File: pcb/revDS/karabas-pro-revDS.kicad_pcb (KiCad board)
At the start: 2 copper layers, 101.6 x 147.3 mm, 212 parts, among them CON1 CF-CARD, CON2 SD, CON3 VGA, CON4 Joystick, CON5 Keyboard, CON6 Mouse, CON7 Audio, CON8 12V, CON9 MicroSD', J1 Floppy, J10 Ext Joystick, J2 FPGA JTAG, J3 Floppy, J4 uBus, J5 AVR JTAG, J6 AVR UART, J7 ESP-BUS, J8 Tape In, J9 Tape Out, Q1 BC856, SW1 SW_Push, SW2 SW_Push, SW4 SW_SPST, U1 EP4CE6E22C8N, U10 ESP-12E, U11 TDA1543, U12 AMS1117-3.3, U13 AMS1117-2.5, U14 AMS1117-1.2, U15 LM2596S-5, U16 LM311, U17 74LS06, U18 74LS38, U2 CY62167EV30, U3 W25Q16, U3''1 W25Q16, U4 EPM3128ATC100-5, U5 ATMEGA328-AU, U6 MB8877A, U7 TXB0104PW, U8 TXB0104PW, U9 DS1307Z+, X1 SG-7050CAN, Y1 32768Hz, Y2 16MHz

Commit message: Updated pcb rev.DS
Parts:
- added G***: LOGO, footprints:karabas_pro_logo2-coppermask, F.Cu at (133.2, 163.9)
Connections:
- net Net-(D1-Pad2) renamed /L1
- net Net-(D2-Pad2) renamed /L2
- net Net-(D4-Pad1) renamed /L4
- net Net-(D6-Pad1) renamed /L5
- net Net-(D7-Pad2) renamed /L3
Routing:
- net VCC1_2: track 132.3 -> 132.9 mm
- net /PIN_25: track 31.7 -> 32.3 mm

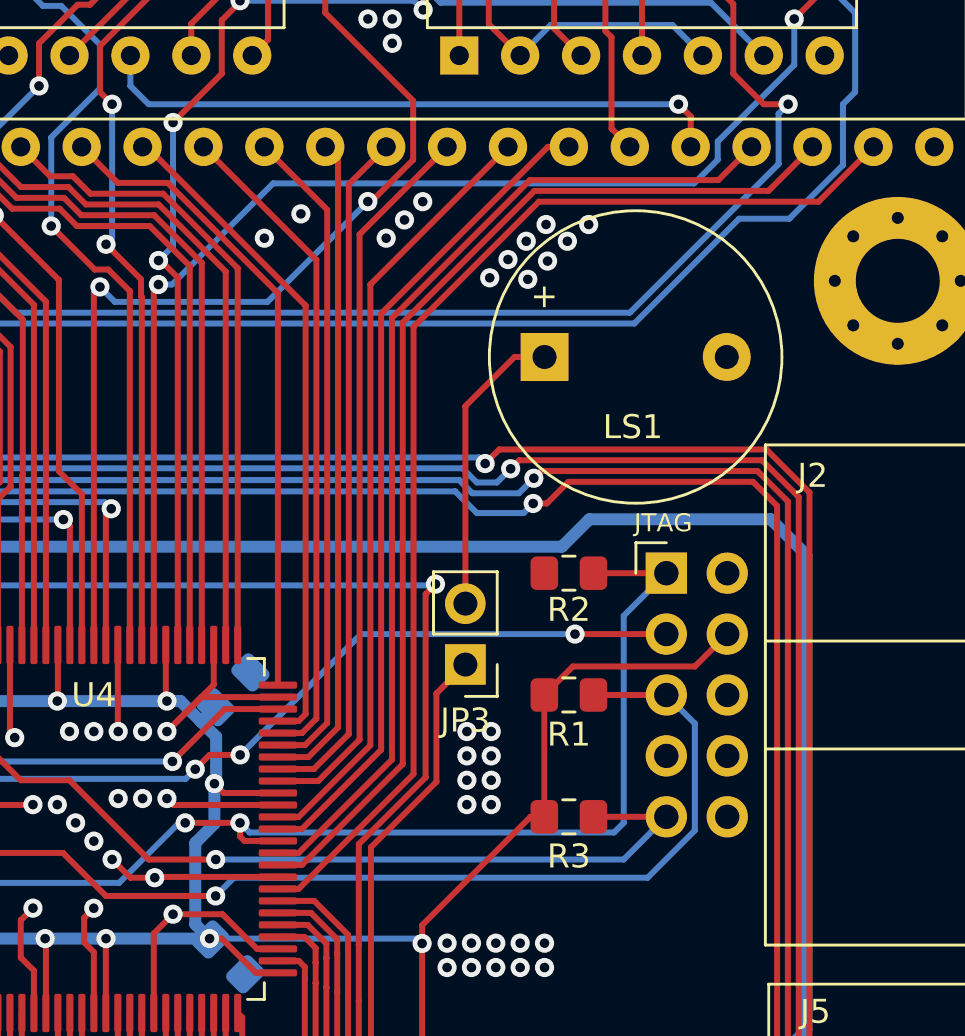
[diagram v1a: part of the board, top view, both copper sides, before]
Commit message: updated revDS: added diode and transistor before buzzer
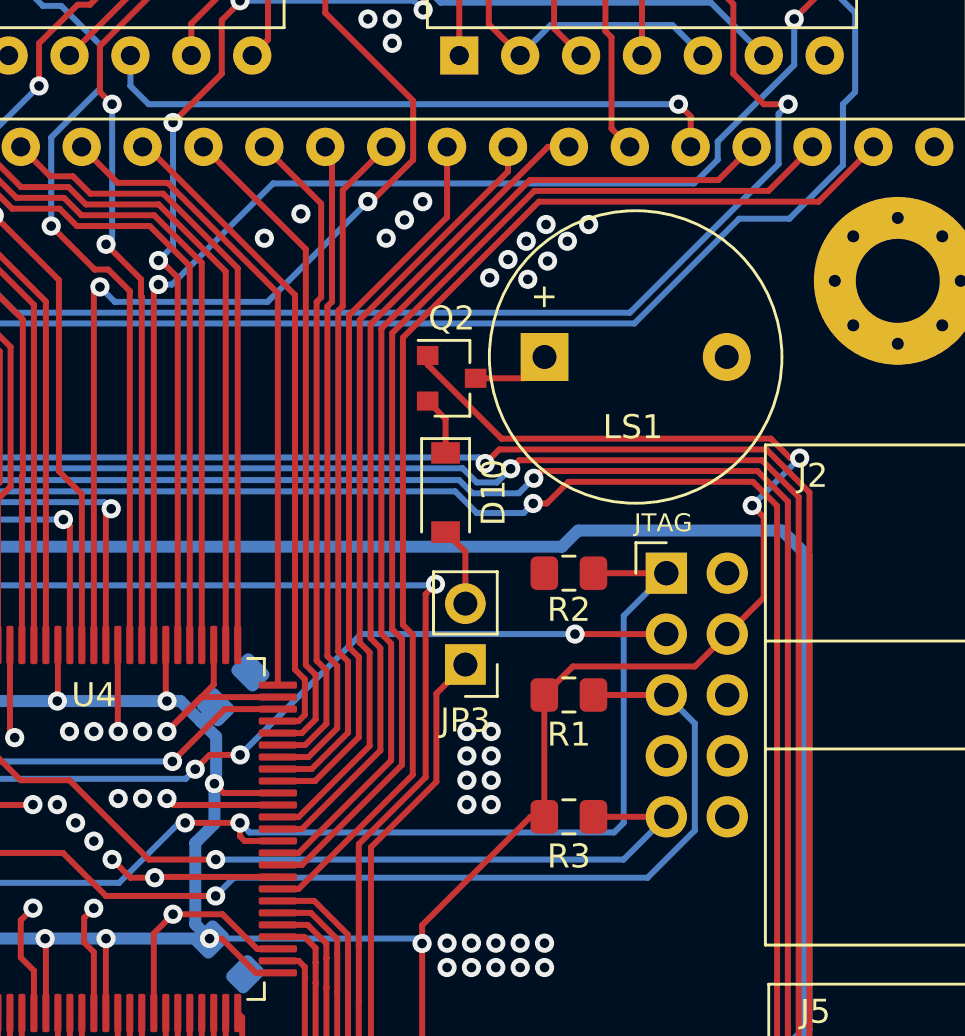
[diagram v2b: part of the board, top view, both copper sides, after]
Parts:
- removed the G*** at (133.2, 163.9)
- added D10: 1N4148W, Diode_SMD:D_SOD-123, F.Cu at (177.7, 79.4)
- added Q2: BC548, Package_TO_SOT_SMD:SOT-23, F.Cu at (178.0, 74.7)
- U1: value EP4CE6E22C8N -> EP4CE10E22C8N
- U2: value CY62167EV30 -> CY62167EV30LL
- U4: value EPM3128ATC100-5 -> EPM3128ATC100-10N
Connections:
- JP3 pad 2: Net-(JP3-Pad2) -> Net-(D10-Pad2)
- LS1 pad 1: Net-(JP3-Pad2) -> Net-(LS1-Pad1)
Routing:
- net VCC3_3: track 616.0 -> 642.5 mm, vias 39 -> 41
- net Net-(JP3-Pad2): track 13.1 -> 0.00 mm
- net Net-(LS1-Pad1): track 0.00 -> 3.75 mm
- net Net-(D10-Pad2): track 0.00 -> 3.33 mm
- net Net-(D10-Pad1): track 0.00 -> 2.47 mm

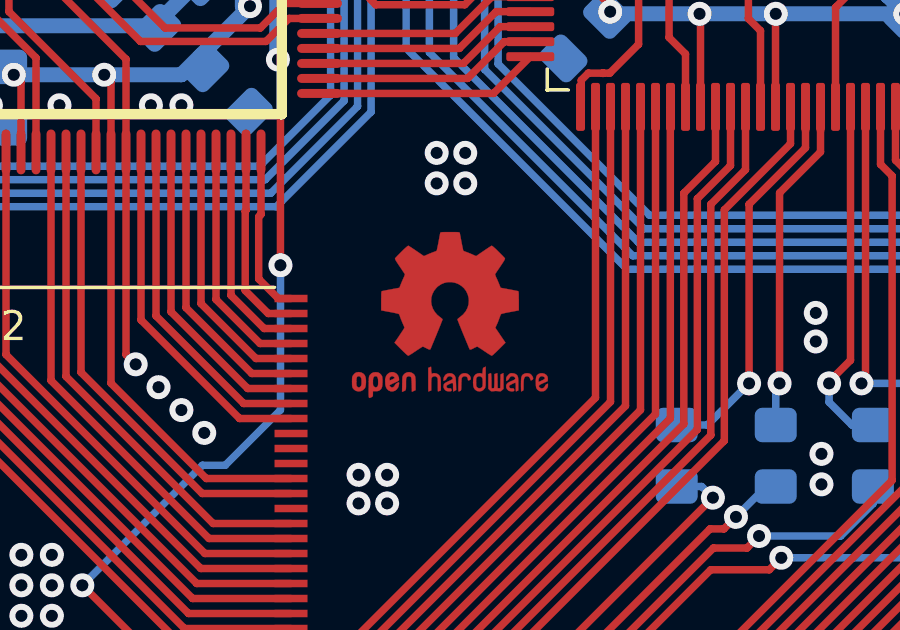
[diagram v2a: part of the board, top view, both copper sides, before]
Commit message: OSH logo - mask
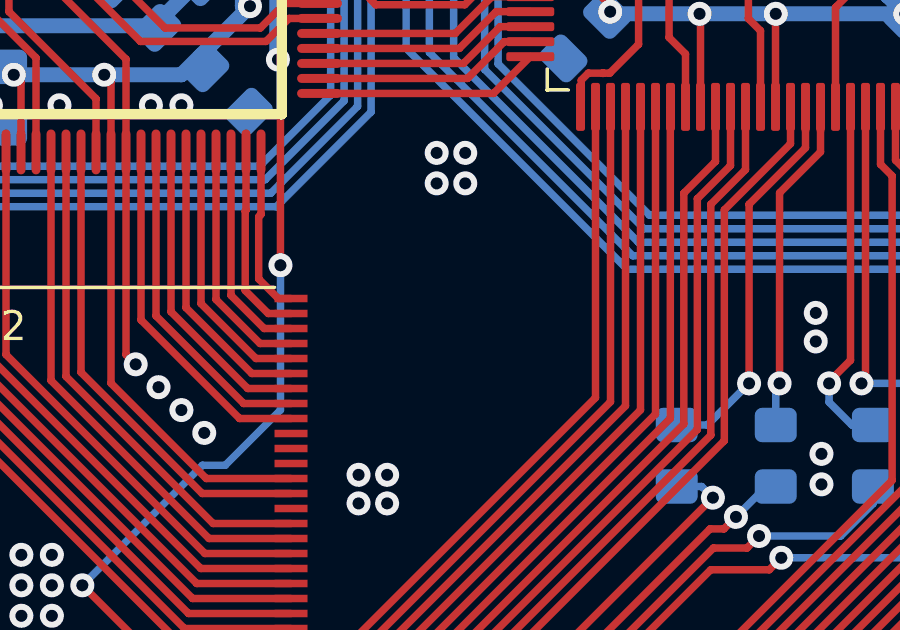
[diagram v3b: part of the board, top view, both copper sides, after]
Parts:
- REF**: value OSHW-Logo2_7.3x6mm_Copper -> OSHW-Logo2_7.3x6mm_Mask; footprint Symbol:OSHW-Logo2_7.3x6mm_Copper -> footprints:OSHW-Logo2_7.3x6mm_Mask

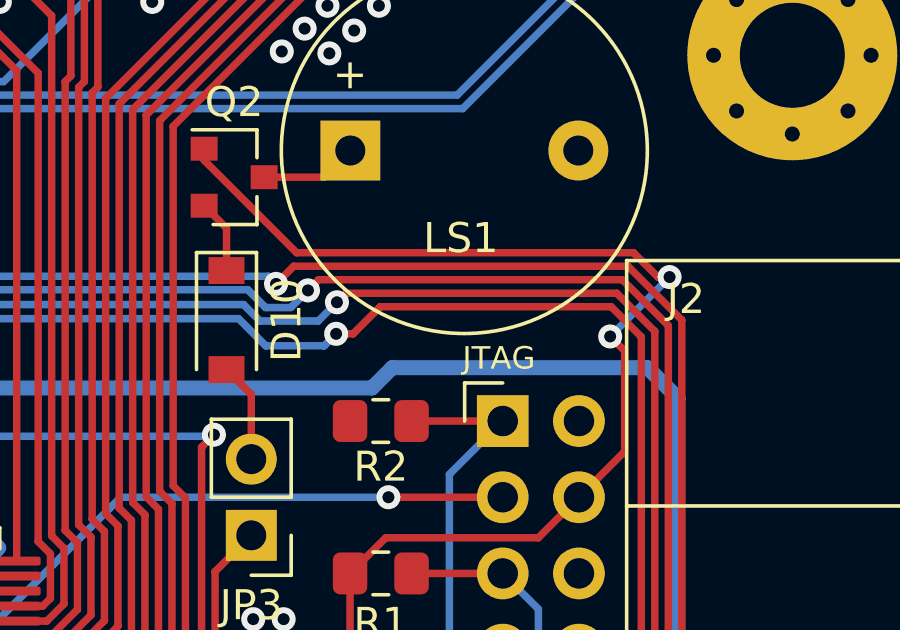
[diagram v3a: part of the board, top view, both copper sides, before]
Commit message: Added missing R for buzzer
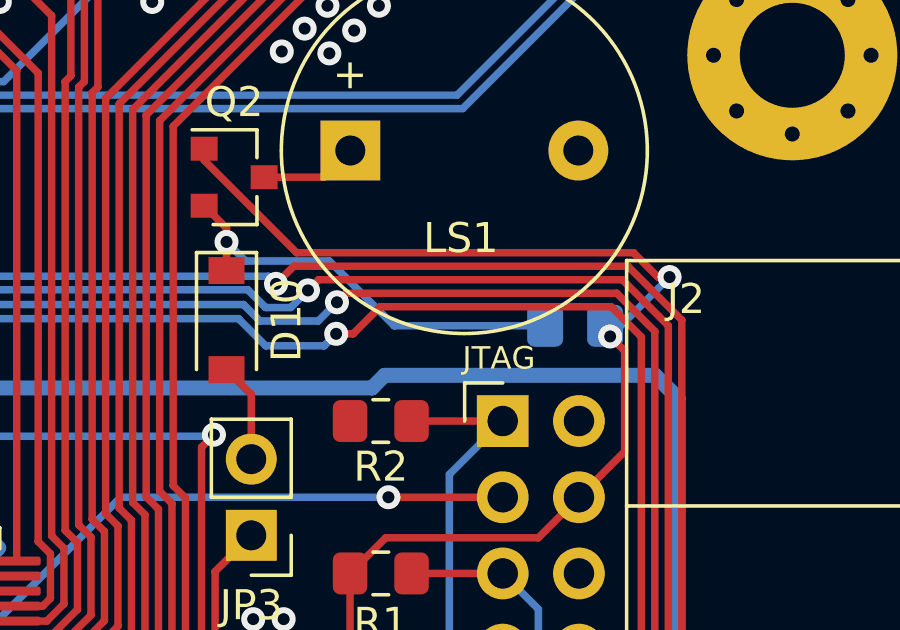
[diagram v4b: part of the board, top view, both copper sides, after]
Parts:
- added R48: 1k, Resistor_SMD:R_0805_2012Metric_Pad1.20x1.40mm_HandSolder, B.Cu at (189.4, 79.6)
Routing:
- net Net-(D10-Pad1): track 2.47 -> 14.2 mm, vias 0 -> 1

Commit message: latest version
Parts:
- added C59: 1uF, Capacitor_SMD:C_0805_2012Metric_Pad1.18x1.45mm_HandSolder, F.Cu at (216.3, 124.6)
- added C60: 1uF, Capacitor_SMD:C_0805_2012Metric_Pad1.18x1.45mm_HandSolder, F.Cu at (221.2, 124.6)
- added C61: 1uF, Capacitor_SMD:C_0805_2012Metric_Pad1.18x1.45mm_HandSolder, F.Cu at (216.3, 127.6)
- added C62: 1uF, Capacitor_SMD:C_0805_2012Metric_Pad1.18x1.45mm_HandSolder, F.Cu at (221.2, 127.6)
- added U19: AMS1117-3.3, Package_TO_SOT_SMD:TO-252-2, F.Cu at (220.0, 119.1)
- added U20: AMS1117-3.3, Package_TO_SOT_SMD:TO-252-2, F.Cu at (232.2, 119.1)
- C27: moved to F.Cu
- moved C27 11.3 mm to (124.7, 113.0), turned to 225 degrees
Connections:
- C13 pad 1: VCC3_3 -> /+3.3ESP
- C18 pad 1: VCC3_3 -> /+3.3ESP
- C54 pad 1: VCC3_3 -> /+3.3ESP
- CON1 pad 13: VCC3_3 -> +3.3VP
- CON1 pad 38: VCC3_3 -> +3.3VP
- CON2 pad 4: VCC3_3 -> +3.3VP
- CON9 pad 4: VCC3_3 -> +3.3VP
- D4 pad 2: VCC3_3 -> +3.3VP
- D6 pad 2: VCC3_3 -> +3.3VP
- J7 pad 10: VCC3_3 -> /+3.3ESP
- R30 pad 2: VCC3_3 -> /+3.3ESP
- R31 pad 2: VCC3_3 -> /+3.3ESP
- R36 pad 2: VCC3_3 -> +3.3VP
- R37 pad 1: VCC3_3 -> +3.3VP
- R52 pad 2: VCC3_3 -> +3.3VP
- R74 pad 1: VCC3_3 -> +3.3VP
- R75 pad 1: VCC3_3 -> +3.3VP
- U10 pad 8: VCC3_3 -> /+3.3ESP
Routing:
- net VCC3_3: track 642.5 -> 405.1 mm, vias 41 -> 29
- net +3.3VP: track 0.00 -> 84.5 mm, vias 0 -> 3
- net /+3.3ESP: track 0.00 -> 45.1 mm
- net VCC: track 650.9 -> 651.4 mm

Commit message: Revert "latest version"
This reverts commit fe14166d25968ab133076a7a9191b22261ce910e.
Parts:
- removed C59, C60, C61, C62: 1uF, Capacitor_SMD:C_0805_2012Metric_Pad1.18x1.45mm_HandSolder
- removed U19, U20: AMS1117-3.3, Package_TO_SOT_SMD:TO-252-2
- C27: moved to B.Cu
- moved C27 11.3 mm to (135.3, 117.0), turned to 90 degrees
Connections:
- C13 pad 1: /+3.3ESP -> VCC3_3
- C18 pad 1: /+3.3ESP -> VCC3_3
- C54 pad 1: /+3.3ESP -> VCC3_3
- CON1 pad 13: +3.3VP -> VCC3_3
- CON1 pad 38: +3.3VP -> VCC3_3
- CON2 pad 4: +3.3VP -> VCC3_3
- CON9 pad 4: +3.3VP -> VCC3_3
- D4 pad 2: +3.3VP -> VCC3_3
- D6 pad 2: +3.3VP -> VCC3_3
- J7 pad 10: /+3.3ESP -> VCC3_3
- R30 pad 2: /+3.3ESP -> VCC3_3
- R31 pad 2: /+3.3ESP -> VCC3_3
- R36 pad 2: +3.3VP -> VCC3_3
- R37 pad 1: +3.3VP -> VCC3_3
- R52 pad 2: +3.3VP -> VCC3_3
- R74 pad 1: +3.3VP -> VCC3_3
- R75 pad 1: +3.3VP -> VCC3_3
- U10 pad 8: /+3.3ESP -> VCC3_3
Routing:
- net VCC3_3: track 405.1 -> 642.5 mm, vias 29 -> 41
- net +3.3VP: track 84.5 -> 0.00 mm, vias 3 -> 0
- net /+3.3ESP: track 45.1 -> 0.00 mm
- net VCC: track 651.4 -> 650.9 mm
